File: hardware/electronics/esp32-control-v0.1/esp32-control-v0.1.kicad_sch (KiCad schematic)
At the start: 16 parts, among them J1 USB-C POWER + DATA, J2 BATTERY MX1.25 LOCK 2P, J3 M6 SENSOR 10-30V MX1.25 2P, J4 M6 CARRIER HOST MX1.25 LOCK 8P, J5 PVDF ADC AUX MX1.25, J6 PVDF COMPARATOR AUX MX1.25 2P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, J7 UI PANEL MX1.25 LOCK 12P, J8 M6 SENSOR RAIL MX1.25 2P, SW1 POWER / START KEY, U1 ESP32-S3-WROOM-1-N16R8, U2 IP5305T-HSOP8-1EP / 1S POWER, U3 TPS62162DSG / 3V3 BUCK

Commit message: 🔌 统一 Type-C 充电入口
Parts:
- removed J1: USB-C POWER + DATA, Connector_USB:GCT_USB4105-xx-A_16P_TopMnt_Horizontal, symbol Connector:USB_C_Receptacle_USB2.0_16P
- removed J7: UI PANEL MX1.25 LOCK 12P, Connector_JST:JST_GH_SM12B-GHS-TB_1x12-1MP_P1.25mm_Horizontal, symbol Connector_Generic:Conn_01x12
- added J7: UI PANEL MX1.25 LOCK 14P / CHARGE VBUS, Connector_JST:JST_GH_SM14B-GHS-TB_1x14-1MP_P1.25mm_Horizontal, symbol Connector_Generic:Conn_01x14
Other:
- note added: "J4: MX1.25 keyed harness to M6 carrier; J7: 14-pin keyed UI daughter cable with VBUS/GND"
- note added: "The y+ UI-panel Type-C is the sole external charge input; J7 pins 13/14 carry VBUS/GND to the mother-board PTC"
- note removed: "J1 USB-C: VBUS + D+/D-; ESD/PTC and CC pulldowns are on the mother PCB"
- note removed: "J4: MX1.25 keyed harness to M6 carrier; J7: MX1.25 keyed UI daughter board"
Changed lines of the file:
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@@
 		(effects (font (size 2 2)) (justify left bottom))
 	)
-	(text "J1 USB-C: VBUS + D+/D-; ESD/PTC and CC pulldowns are on the mother PCB"
+	(text "The y+ UI-panel Type-C is the sole external charge input; J7 pins 13/14 carry VBUS/GND to the mother-board PTC"
 		(exclude_from_sim no)
 		(at 12 22 0)
@@
 		(effects (font (size 1.27 1.27)) (justify left bottom))
 	)
-	(text "J4: MX1.25 keyed harness to M6 carrier; J7: MX1.25 keyed UI daughter board"
+	(text "J4: MX1.25 keyed harness to M6 carrier; J7: 14-pin keyed UI daughter cable with VBUS/GND"
 		(exclude_from_sim no)
 		(at 116 28 0)
@@
 		)
 	)
-	(label "VBUS_USB_C"
+	(label "VBUS_FROM_UI_TYPEC"
 		(at 43 42 0)
 		(effects
@@
 		(instances
 			(project "esp32-control-v0.1"
-				(path "/9fe79e85-e68f-4910-88f2-38181d01ff34"
+				(path "/e3cf5993-24f8-46a8-8167-70febe176988"
 					(reference "U1")
-					(unit 1)
-				)
-			)
-		)
-	)
-	(symbol
-		(lib_id "Connector:USB_C_Receptacle_USB2.0_16P")
-		(at 28 50 0)
-		(unit 1)
-		(exclude_from_sim no)
-		(in_bom yes)
-		(on_board yes)
-		(dnp no)
-		(property "Reference" "J1"
-			(at 0 -3.81 0)
-			(effects
-				(font
-					(size 1.27 1.27)
-				)
-			)
-		)
-		(property "Value" "USB-C POWER + DATA"
-			(at 0 3.81 0)
-			(effects
-				(font
-					(size 1.27 1.27)
-				)
-			)
-		)
-		(property "Footprint" "Connector_USB:GCT_USB4105-xx-A_16P_TopMnt_Horizontal"
-			(at 0 0 0)
-			(effects
-				(font
-					(size 1.27 1.27)
-				)
-				(hide yes)
-			)
-		)
-		(property "Datasheet" "~"
-			(at 0 0 0)
-			(effects
-				(font
-					(size 1.27 1.27)
-				)
-				(hide yes)
-			)
-		)
-		(property "Description" "Pingpang SmartGear connectorized control path"
-			(at 0 0 0)
-			(effects
-				(font
-					(size 1.27 1.27)
-				)
-				(hide yes)
-			)
-		)
-		(pin "A1"
-		)
-		(pin "A4"
-		)
-		(pin "A5"
-		)
-		(pin "A6"
-		)
-		(pin "A7"
-		)
-		(pin "A8"
-		)
-		(pin "A9"
-		)
-		(pin "A12"
-		)
-		(pin "B1"
-		)
-		(pin "B4"
-		)
-		(pin "B5"
-		)
-		(pin "B6"
-		)
-		(pin "B7"
-		)
-		(pin "B8"
-		)
-		(pin "B9"
-		)
-		(pin "B12"
-		)
-		(pin "SH"
-		)
-		(instances
-			(project "esp32-control-v0.1"
-				(path "/9fe79e85-e68f-4910-88f2-38181d01ff34"
-					(reference "J1")
 					(unit 1)
 				)
@@
 		(instances
 			(project "esp32-control-v0.1"
-				(path "/9fe79e85-e68f-4910-88f2-38181d01ff34"
+				(path "/e3cf5993-24f8-46a8-8167-70febe176988"
 					(reference "J2")
 					(unit 1)
@@
 		(instances
 			(project "esp32-control-v0.1"
-				(path "/9fe79e85-e68f-4910-88f2-38181d01ff34"
+				(path "/e3cf5993-24f8-46a8-8167-70febe176988"
 					(reference "J3")
 					(unit 1)
@@
 		(instances
 			(project "esp32-control-v0.1"
-				(path "/9fe79e85-e68f-4910-88f2-38181d01ff34"
+				(path "/e3cf5993-24f8-46a8-8167-70febe176988"
 					(reference "J6")
 					(unit 1)
@@
 		(instances
 			(project "esp32-control-v0.1"
-				(path "/9fe79e85-e68f-4910-88f2-38181d01ff34"
+				(path "/e3cf5993-24f8-46a8-8167-70febe176988"
 					(reference "J8")
 					(unit 1)
@@
 		(instances
 			(project "esp32-control-v0.1"
-				(path "/9fe79e85-e68f-4910-88f2-38181d01ff34"
+				(path "/e3cf5993-24f8-46a8-8167-70febe176988"
 					(reference "BT1")
 					(unit 1)
@@
 		(instances
 			(project "esp32-control-v0.1"
-				(path "/9fe79e85-e68f-4910-88f2-38181d01ff34"
+				(path "/e3cf5993-24f8-46a8-8167-70febe176988"
 					(reference "U2")
 					(unit 1)
@@
 		(instances
 			(project "esp32-control-v0.1"
-				(path "/9fe79e85-e68f-4910-88f2-38181d01ff34"
+				(path "/e3cf5993-24f8-46a8-8167-70febe176988"
 					(reference "U3")
 					(unit 1)
@@
 		(instances
 			(project "esp32-control-v0.1"
-				(path "/9fe79e85-e68f-4910-88f2-38181d01ff34"
+				(path "/e3cf5993-24f8-46a8-8167-70febe176988"
 					(reference "J4")
 					(unit 1)
@@
 	)
 	(symbol
-		(lib_id "Connector_Generic:Conn_01x12")
+		(lib_id "Connector_Generic:Conn_01x14")
 		(at 182 125 0)
 		(unit 1)
@@
 			)
 		)
-		(property "Value" "UI PANEL MX1.25 LOCK 12P"
-			(at 0 3.81 0)
-			(effects
-				(font
-					(size 1.27 1.27)
-				)
-			)
-		)
-		(property "Footprint" "Connector_JST:JST_GH_SM12B-GHS-TB_1x12-1MP_P1.25mm_Horizontal"
+		(property "Value" "UI PANEL MX1.25 LOCK 14P / CHARGE VBUS"
+			(at 0 3.81 0)
+			(effects
+				(font
+					(size 1.27 1.27)
+				)
+			)
+		)
+		(property "Footprint" "Connector_JST:JST_GH_SM14B-GHS-TB_1x14-1MP_P1.25mm_Horizontal"
 			(at 0 0 0)
 			(effects
@@
 		(pin "12"
 		)
-		(instances
-			(project "esp32-control-v0.1"
-				(path "/9fe79e85-e68f-4910-88f2-38181d01ff34"
+		(pin "13"
+		)
+		(pin "14"
+		)
+		(instances
+			(project "esp32-control-v0.1"
+				(path "/e3cf5993-24f8-46a8-8167-70febe176988"
 					(reference "J7")
 					(unit 1)
@@
 		(instances
 			(project "esp32-control-v0.1"
-				(path "/9fe79e85-e68f-4910-88f2-38181d01ff34"
+				(path "/e3cf5993-24f8-46a8-8167-70febe176988"
 					(reference "J5")
 					(unit 1)
@@
 		(instances
 			(project "esp32-control-v0.1"
-				(path "/9fe79e85-e68f-4910-88f2-38181d01ff34"
+				(path "/e3cf5993-24f8-46a8-8167-70febe176988"
 					(reference "SW1")
 					(unit 1)
@@
 		(instances
 			(project "esp32-control-v0.1"
-				(path "/9fe79e85-e68f-4910-88f2-38181d01ff34"
+				(path "/e3cf5993-24f8-46a8-8167-70febe176988"
 					(reference "D1")
 					(unit 1)
@@
 		(instances
 			(project "esp32-control-v0.1"
-				(path "/9fe79e85-e68f-4910-88f2-38181d01ff34"
+				(path "/e3cf5993-24f8-46a8-8167-70febe176988"
 					(reference "C1")
 					(unit 1)
@@
 		(instances
 			(project "esp32-control-v0.1"
-				(path "/9fe79e85-e68f-4910-88f2-38181d01ff34"
+				(path "/e3cf5993-24f8-46a8-8167-70febe176988"
 					(reference "C2")
 					(unit 1)
@@
 		(instances
 			(project "esp32-control-v0.1"
-				(path "/9fe79e85-e68f-4910-88f2-38181d01ff34"
+				(path "/e3cf5993-24f8-46a8-8167-70febe176988"
 					(reference "#PWR01")
 					(unit 1)
@@
 		(instances
 			(project "esp32-control-v0.1"
-				(path "/9fe79e85-e68f-4910-88f2-38181d01ff34"
+				(path "/e3cf5993-24f8-46a8-8167-70febe176988"
 					(reference "#PWR02")
 					(unit 1)
@@
 		(instances
 			(project "esp32-control-v0.1"
-				(path "/9fe79e85-e68f-4910-88f2-38181d01ff34"
+				(path "/e3cf5993-24f8-46a8-8167-70febe176988"
 					(reference "#PWR03")
 					(unit 1)

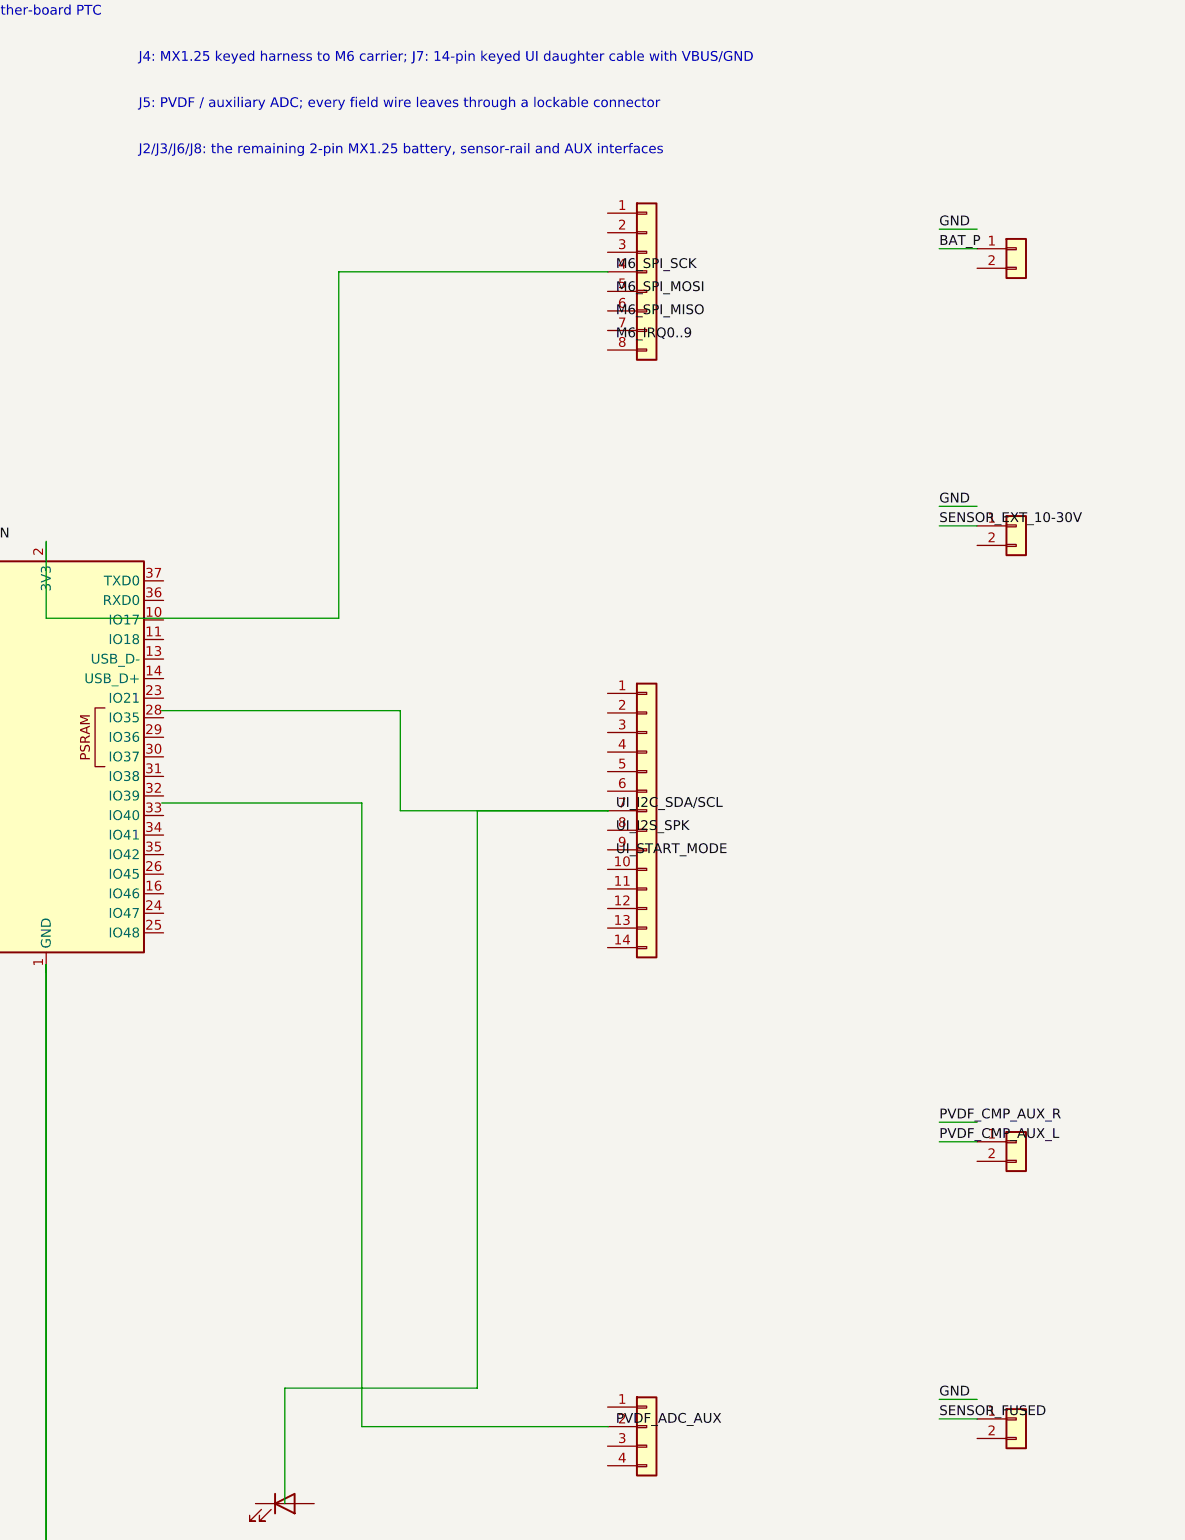
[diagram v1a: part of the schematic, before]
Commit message: 🔌 修复线束契约与电子机械干涉
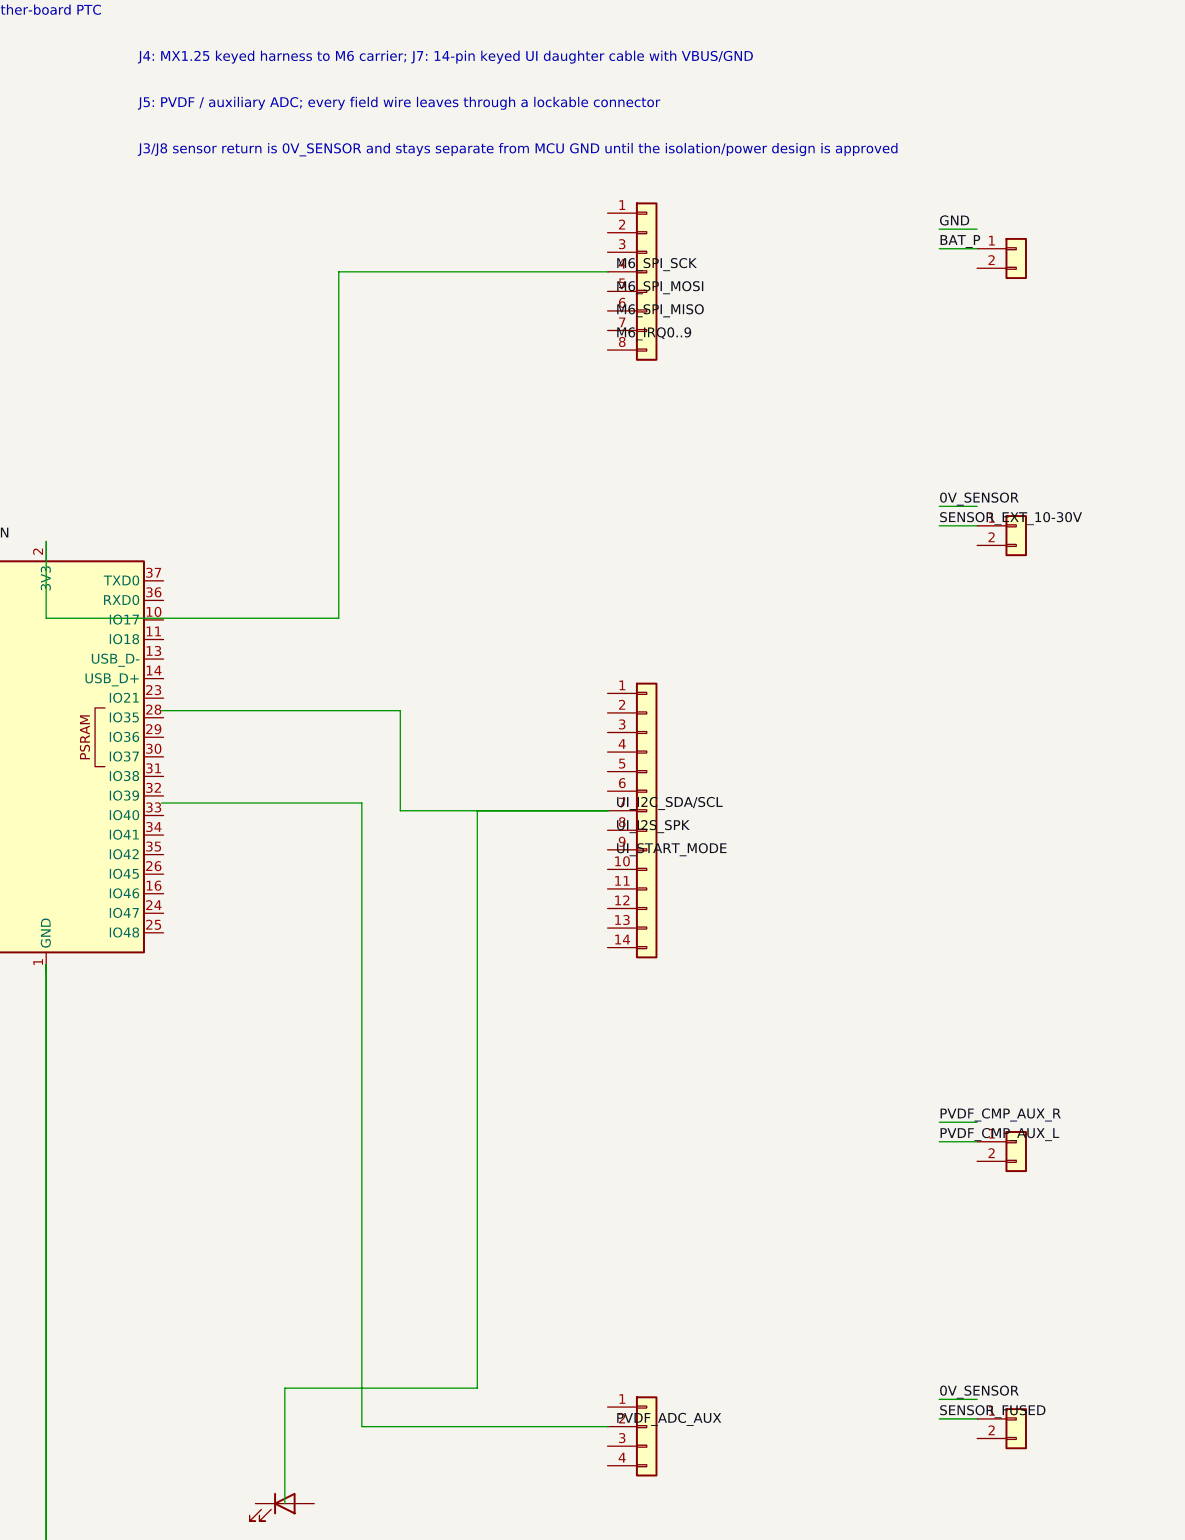
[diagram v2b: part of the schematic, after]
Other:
- note added: "J3/J8 sensor return is 0V_SENSOR and stays separate from MCU GND until the isolation/power design is approved"
- note removed: "J2/J3/J6/J8: the remaining 2-pin MX1.25 battery, sensor-rail and AUX interfaces"
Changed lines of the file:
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@@
 		(effects (font (size 1.27 1.27)) (justify left bottom))
 	)
-	(text "J2/J3/J6/J8: the remaining 2-pin MX1.25 battery, sensor-rail and AUX interfaces"
+	(text "J3/J8 sensor return is 0V_SENSOR and stays separate from MCU GND until the isolation/power design is approved"
 		(exclude_from_sim no)
 		(at 116 40 0)
@@
 		)
 	)
-	(label "GND"
+	(label "0V_SENSOR"
 		(at 220 85.46 0)
 		(effects
@@
 		)
 	)
-	(label "GND"
+	(label "0V_SENSOR"
 		(at 220 201.46 0)
 		(effects
@@
 		(instances
 			(project "esp32-control-v0.1"
-				(path "/e3cf5993-24f8-46a8-8167-70febe176988"
+				(path "/5cac66eb-ff22-48bf-95d5-0db97be6b89f"
 					(reference "U1")
 					(unit 1)
@@
 		(instances
 			(project "esp32-control-v0.1"
-				(path "/e3cf5993-24f8-46a8-8167-70febe176988"
+				(path "/5cac66eb-ff22-48bf-95d5-0db97be6b89f"
 					(reference "J2")
 					(unit 1)
@@
 		(instances
 			(project "esp32-control-v0.1"
-				(path "/e3cf5993-24f8-46a8-8167-70febe176988"
+				(path "/5cac66eb-ff22-48bf-95d5-0db97be6b89f"
 					(reference "J3")
 					(unit 1)
@@
 		(instances
 			(project "esp32-control-v0.1"
-				(path "/e3cf5993-24f8-46a8-8167-70febe176988"
+				(path "/5cac66eb-ff22-48bf-95d5-0db97be6b89f"
 					(reference "J6")
 					(unit 1)
@@
 		(instances
 			(project "esp32-control-v0.1"
-				(path "/e3cf5993-24f8-46a8-8167-70febe176988"
+				(path "/5cac66eb-ff22-48bf-95d5-0db97be6b89f"
 					(reference "J8")
 					(unit 1)
@@
 		(instances
 			(project "esp32-control-v0.1"
-				(path "/e3cf5993-24f8-46a8-8167-70febe176988"
+				(path "/5cac66eb-ff22-48bf-95d5-0db97be6b89f"
 					(reference "BT1")
 					(unit 1)
@@
 		(instances
 			(project "esp32-control-v0.1"
-				(path "/e3cf5993-24f8-46a8-8167-70febe176988"
+				(path "/5cac66eb-ff22-48bf-95d5-0db97be6b89f"
 					(reference "U2")
 					(unit 1)
@@
 		(instances
 			(project "esp32-control-v0.1"
-				(path "/e3cf5993-24f8-46a8-8167-70febe176988"
+				(path "/5cac66eb-ff22-48bf-95d5-0db97be6b89f"
 					(reference "U3")
 					(unit 1)
@@
 		(instances
 			(project "esp32-control-v0.1"
-				(path "/e3cf5993-24f8-46a8-8167-70febe176988"
+				(path "/5cac66eb-ff22-48bf-95d5-0db97be6b89f"
 					(reference "J4")
 					(unit 1)
@@
 		(instances
 			(project "esp32-control-v0.1"
-				(path "/e3cf5993-24f8-46a8-8167-70febe176988"
+				(path "/5cac66eb-ff22-48bf-95d5-0db97be6b89f"
 					(reference "J7")
 					(unit 1)
@@
 		(instances
 			(project "esp32-control-v0.1"
-				(path "/e3cf5993-24f8-46a8-8167-70febe176988"
+				(path "/5cac66eb-ff22-48bf-95d5-0db97be6b89f"
 					(reference "J5")
 					(unit 1)
@@
 		(instances
 			(project "esp32-control-v0.1"
-				(path "/e3cf5993-24f8-46a8-8167-70febe176988"
+				(path "/5cac66eb-ff22-48bf-95d5-0db97be6b89f"
 					(reference "SW1")
 					(unit 1)
@@
 		(instances
 			(project "esp32-control-v0.1"
-				(path "/e3cf5993-24f8-46a8-8167-70febe176988"
+				(path "/5cac66eb-ff22-48bf-95d5-0db97be6b89f"
 					(reference "D1")
 					(unit 1)
@@
 		(instances
 			(project "esp32-control-v0.1"
-				(path "/e3cf5993-24f8-46a8-8167-70febe176988"
+				(path "/5cac66eb-ff22-48bf-95d5-0db97be6b89f"
 					(reference "C1")
 					(unit 1)
@@
 		(instances
 			(project "esp32-control-v0.1"
-				(path "/e3cf5993-24f8-46a8-8167-70febe176988"
+				(path "/5cac66eb-ff22-48bf-95d5-0db97be6b89f"
 					(reference "C2")
 					(unit 1)
@@
 		(instances
 			(project "esp32-control-v0.1"
-				(path "/e3cf5993-24f8-46a8-8167-70febe176988"
+				(path "/5cac66eb-ff22-48bf-95d5-0db97be6b89f"
 					(reference "#PWR01")
 					(unit 1)
@@
 		(instances
 			(project "esp32-control-v0.1"
-				(path "/e3cf5993-24f8-46a8-8167-70febe176988"
+				(path "/5cac66eb-ff22-48bf-95d5-0db97be6b89f"
 					(reference "#PWR02")
 					(unit 1)
@@
 		(instances
 			(project "esp32-control-v0.1"
-				(path "/e3cf5993-24f8-46a8-8167-70febe176988"
+				(path "/5cac66eb-ff22-48bf-95d5-0db97be6b89f"
 					(reference "#PWR03")
 					(unit 1)
